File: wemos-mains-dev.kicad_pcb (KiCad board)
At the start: 2 copper layers, 74.2 x 46.5 mm, 15 parts, among them J1 Screw_Terminal_01x02, J2 Conn_02x12_Odd_Even, J8 SDA PU, J9 SDA PU, U1 AC-05-3, U2 WeMos_D1_mini

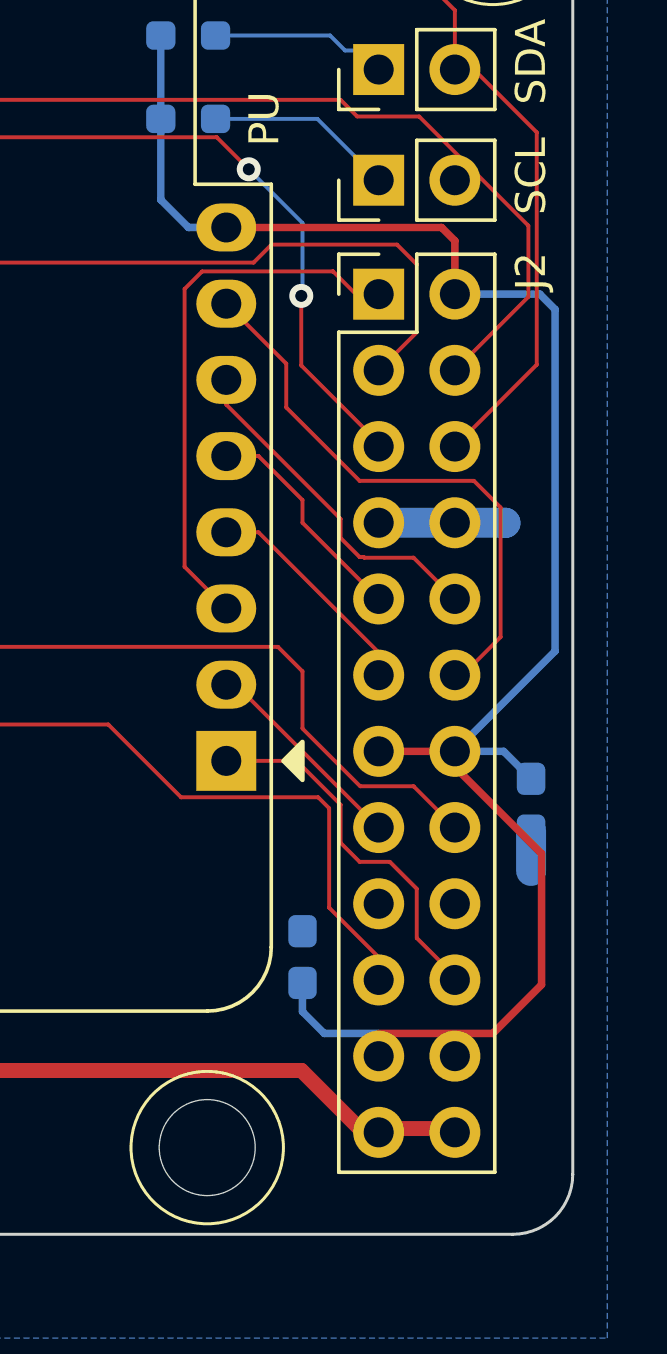
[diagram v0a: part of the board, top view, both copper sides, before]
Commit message: changed hat socket to socket from header
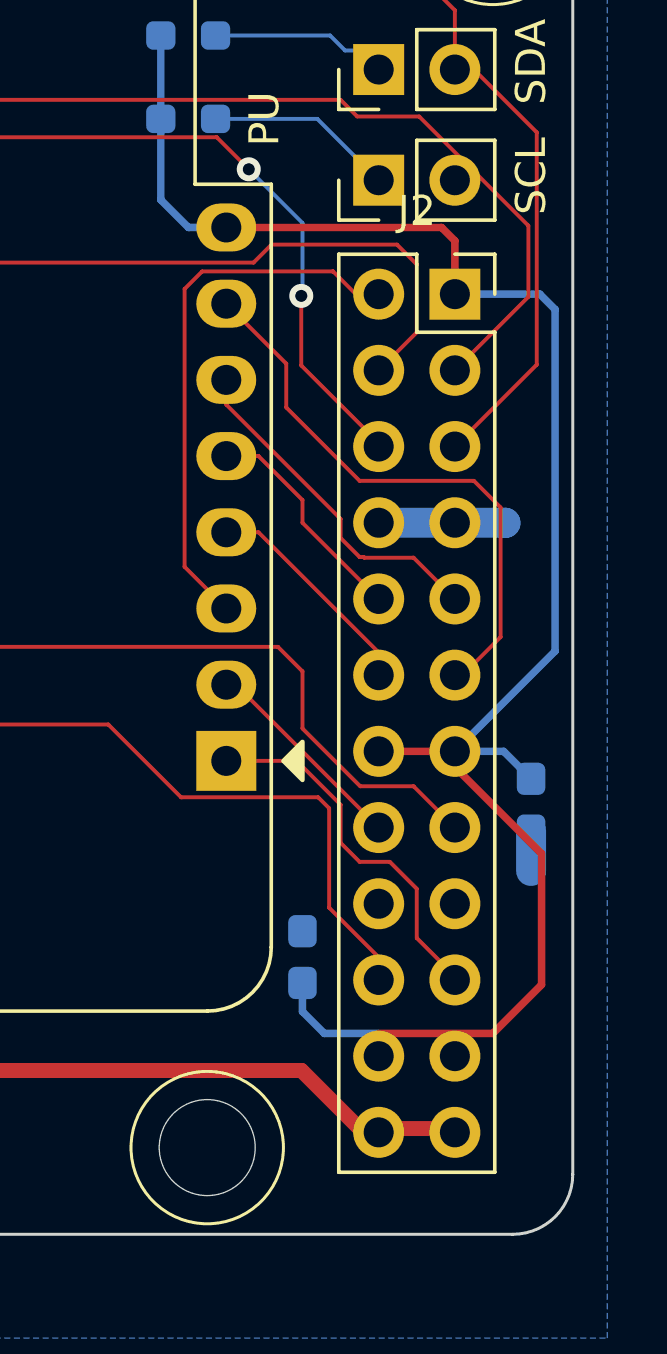
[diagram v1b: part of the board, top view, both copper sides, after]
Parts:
- J2: footprint Connector_PinHeader_2.54mm:PinHeader_2x12_P2.54mm_Vertical -> Connector_PinSocket_2.54mm:PinSocket_2x12_P2.54mm_Vertical
- moved J2 2.54 mm to (137.2, 87.1)
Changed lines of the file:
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@@
     (pad "" np_thru_hole circle (at 0 0) (size 3.2 3.2) (drill 3.2) (layers "*.Cu" "*.Mask"))
   )
-  (footprint "Connector_PinHeader_2.54mm:PinHeader_2x12_P2.54mm_Vertical" (layer "F.Cu")
-    (at 134.62 87.122)
-    (descr "Through hole straight pin header, 2x12, 2.54mm pitch, double rows")
-    (tags "Through hole pin header THT 2x12 2.54mm double row")
+  (footprint "Connector_PinSocket_2.54mm:PinSocket_2x12_P2.54mm_Vertical" (layer "F.Cu")
+    (at 137.16 87.122)
+    (descr "Through hole straight socket strip, 2x12, 2.54mm pitch, double cols (from Kicad 4.0.7), script generated")
+    (tags "Through hole socket strip THT 2x12 2.54mm double row")
     (property "Sheetfile" "wemos-mains-dev.kicad_sch")
     (property "Sheetname" "")
@@
     (property "ki_keywords" "connector")
     (attr through_hole)
-    (fp_text reference "J2" (at 5.08 -0.762 90) (layer "F.SilkS")
+    (fp_text reference "J2" (at -1.27 -2.77) (layer "F.SilkS")
         (effects (font (size 1 1) (thickness 0.15)))
     )
-    (fp_text value "Conn_02x12_Odd_Even" (at -3.65 30.318) (layer "F.Fab")
+    (fp_text value "Conn_02x12_Odd_Even" (at -1.27 30.71) (layer "F.Fab")
         (effects (font (size 1 1) (thickness 0.15)))
     )
-    (fp_text user "${REFERENCE}" (at 1.27 13.97 90) (layer "F.Fab")
+    (fp_text user "${REFERENCE}" (at -1.27 13.97 90) (layer "F.Fab")
         (effects (font (size 1 1) (thickness 0.15)))
     )
-    (fp_line (start -1.33 -1.33) (end 0 -1.33)
+    (fp_line (start -3.87 -1.33) (end -3.87 29.27)
       (stroke (width 0.12) (type solid)) (layer "F.SilkS"))
-    (fp_line (start -1.33 0) (end -1.33 -1.33)
+    (fp_line (start -3.87 -1.33) (end -1.27 -1.33)
       (stroke (width 0.12) (type solid)) (layer "F.SilkS"))
-    (fp_line (start -1.33 1.27) (end -1.33 29.27)
+    (fp_line (start -3.87 29.27) (end 1.33 29.27)
       (stroke (width 0.12) (type solid)) (layer "F.SilkS"))
-    (fp_line (start -1.33 1.27) (end 1.27 1.27)
+    (fp_line (start -1.27 -1.33) (end -1.27 1.27)
       (stroke (width 0.12) (type solid)) (layer "F.SilkS"))
-    (fp_line (start -1.33 29.27) (end 3.87 29.27)
+    (fp_line (start -1.27 1.27) (end 1.33 1.27)
       (stroke (width 0.12) (type solid)) (layer "F.SilkS"))
-    (fp_line (start 1.27 -1.33) (end 3.87 -1.33)
+    (fp_line (start 0 -1.33) (end 1.33 -1.33)
       (stroke (width 0.12) (type solid)) (layer "F.SilkS"))
-    (fp_line (start 1.27 1.27) (end 1.27 -1.33)
+    (fp_line (start 1.33 -1.33) (end 1.33 0)
       (stroke (width 0.12) (type solid)) (layer "F.SilkS"))
-    (fp_line (start 3.87 -1.33) (end 3.87 29.27)
+    (fp_line (start 1.33 1.27) (end 1.33 29.27)
       (stroke (width 0.12) (type solid)) (layer "F.SilkS"))
-    (fp_line (start -1.8 -1.8) (end -1.8 29.75)
+    (fp_line (start -4.34 -1.8) (end 1.76 -1.8)
       (stroke (width 0.05) (type solid)) (layer "F.CrtYd"))
-    (fp_line (start -1.8 29.75) (end 4.35 29.75)
+    (fp_line (start -4.34 29.7) (end -4.34 -1.8)
       (stroke (width 0.05) (type solid)) (layer "F.CrtYd"))
-    (fp_line (start 4.35 -1.8) (end -1.8 -1.8)
+    (fp_line (start 1.76 -1.8) (end 1.76 29.7)
       (stroke (width 0.05) (type solid)) (layer "F.CrtYd"))
-    (fp_line (start 4.35 29.75) (end 4.35 -1.8)
+    (fp_line (start 1.76 29.7) (end -4.34 29.7)
       (stroke (width 0.05) (type solid)) (layer "F.CrtYd"))
-    (fp_line (start -1.27 0) (end 0 -1.27)
+    (fp_line (start -3.81 -1.27) (end 0.27 -1.27)
       (stroke (width 0.1) (type solid)) (layer "F.Fab"))
-    (fp_line (start -1.27 29.21) (end -1.27 0)
+    (fp_line (start -3.81 29.21) (end -3.81 -1.27)
       (stroke (width 0.1) (type solid)) (layer "F.Fab"))
-    (fp_line (start 0 -1.27) (end 3.81 -1.27)
+    (fp_line (start 0.27 -1.27) (end 1.27 -0.27)
       (stroke (width 0.1) (type solid)) (layer "F.Fab"))
-    (fp_line (start 3.81 -1.27) (end 3.81 29.21)
+    (fp_line (start 1.27 -0.27) (end 1.27 29.21)
       (stroke (width 0.1) (type solid)) (layer "F.Fab"))
-    (fp_line (start 3.81 29.21) (end -1.27 29.21)
+    (fp_line (start 1.27 29.21) (end -3.81 29.21)
       (stroke (width 0.1) (type solid)) (layer "F.Fab"))
     (pad "1" thru_hole rect (at 0 0) (size 1.7 1.7) (drill 1) (layers "*.Cu" "*.Mask")
       (net 7 "D0_GPIO") (pinfunction "Pin_1") (pintype "passive"))
-    (pad "2" thru_hole oval (at 2.54 0) (size 1.7 1.7) (drill 1) (layers "*.Cu" "*.Mask")
+    (pad "2" thru_hole oval (at -2.54 0) (size 1.7 1.7) (drill 1) (layers "*.Cu" "*.Mask")
       (net 1 "+3.3V") (pinfunction "Pin_2") (pintype "passive"))
     (pad "3" thru_hole oval (at 0 2.54) (size 1.7 1.7) (drill 1) (layers "*.Cu" "*.Mask")
       (net 17 "RX") (pinfunction "Pin_3") (pintype "passive"))
-    (pad "4" thru_hole oval (at 2.54 2.54) (size 1.7 1.7) (drill 1) (layers "*.Cu" "*.Mask")
+    (pad "4" thru_hole oval (at -2.54 2.54) (size 1.7 1.7) (drill 1) (layers "*.Cu" "*.Mask")
       (net 15 "D1_SCL") (pinfunction "Pin_4") (pintype "passive"))
     (pad "5" thru_hole oval (at 0 5.08) (size 1.7 1.7) (drill 1) (layers "*.Cu" "*.Mask")
       (net 18 "TX") (pinfunction "Pin_5") (pintype "passive"))
-    (pad "6" thru_hole oval (at 2.54 5.08) (size 1.7 1.7) (drill 1) (layers "*.Cu" "*.Mask")
+    (pad "6" thru_hole oval (at -2.54 5.08) (size 1.7 1.7) (drill 1) (layers "*.Cu" "*.Mask")
       (net 16 "D2_SDA") (pinfunction "Pin_6") (pintype "passive"))
     (pad "7" thru_hole oval (at 0 7.62) (size 1.7 1.7) (drill 1) (layers "*.Cu" "*.Mask")
       (net 3 "GND") (pinfunction "Pin_7") (pintype "passive"))
-    (pad "8" thru_hole oval (at 2.54 7.62) (size 1.7 1.7) (drill 1) (layers "*.Cu" "*.Mask")
+    (pad "8" thru_hole oval (at -2.54 7.62) (size 1.7 1.7) (drill 1) (layers "*.Cu" "*.Mask")
       (net 3 "GND") (pinfunction "Pin_8") (pintype "passive"))
     (pad "9" thru_hole oval (at 0 10.16) (size 1.7 1.7) (drill 1) (layers "*.Cu" "*.Mask")
       (net 10 "D6_MISO") (pinfunction "Pin_9") (pintype "passive"))
-    (pad "10" thru_hole oval (at 2.54 10.16) (size 1.7 1.7) (drill 1) (layers "*.Cu" "*.Mask")
+    (pad "10" thru_hole oval (at -2.54 10.16) (size 1.7 1.7) (drill 1) (layers "*.Cu" "*.Mask")
       (net 13 "D7_MOSI") (pinfunction "Pin_10") (pintype "passive"))
     (pad "11" thru_hole oval (at 0 12.7) (size 1.7 1.7) (drill 1) (layers "*.Cu" "*.Mask")
       (net 9 "D5_SCK") (pinfunction "Pin_11") (pintype "passive"))
-    (pad "12" thru_hole oval (at 2.54 12.7) (size 1.7 1.7) (drill 1) (layers "*.Cu" "*.Mask")
+    (pad "12" thru_hole oval (at -2.54 12.7) (size 1.7 1.7) (drill 1) (layers "*.Cu" "*.Mask")
       (net 14 "D8_CS") (pinfunction "Pin_12") (pintype "passive"))
     (pad "13" thru_hole oval (at 0 15.24) (size 1.7 1.7) (drill 1) (layers "*.Cu" "*.Mask")
       (net 1 "+3.3V") (pinfunction "Pin_13") (pintype "passive"))
-    (pad "14" thru_hole oval (at 2.54 15.24) (size 1.7 1.7) (drill 1) (layers "*.Cu" "*.Mask")
+    (pad "14" thru_hole oval (at -2.54 15.24) (size 1.7 1.7) (drill 1) (layers "*.Cu" "*.Mask")
       (net 1 "+3.3V") (pinfunction "Pin_14") (pintype "passive"))
     (pad "15" thru_hole oval (at 0 17.78) (size 1.7 1.7) (drill 1) (layers "*.Cu" "*.Mask")
       (net 21 "A0_ANL") (pinfunction "Pin_15") (pintype "passive"))
-    (pad "16" thru_hole oval (at 2.54 17.78) (size 1.7 1.7) (drill 1) (layers "*.Cu" "*.Mask")
+    (pad "16" thru_hole oval (at -2.54 17.78) (size 1.7 1.7) (drill 1) (layers "*.Cu" "*.Mask")
       (net 12 "D4_LED") (pinfunction "Pin_16") (pintype "passive"))
     (pad "17" thru_hole oval (at 0 20.32) (size 1.7 1.7) (drill 1) (layers "*.Cu" "*.Mask")
       (net 3 "GND") (pinfunction "Pin_17") (pintype "passive"))
-    (pad "18" thru_hole oval (at 2.54 20.32) (size 1.7 1.7) (drill 1) (layers "*.Cu" "*.Mask")
+    (pad "18" thru_hole oval (at -2.54 20.32) (size 1.7 1.7) (drill 1) (layers "*.Cu" "*.Mask")
       (net 3 "GND") (pinfunction "Pin_18") (pintype "passive"))
     (pad "19" thru_hole oval (at 0 22.86) (size 1.7 1.7) (drill 1) (layers "*.Cu" "*.Mask")
       (net 8 "D3_ONE") (pinfunction "Pin_19") (pintype "passive"))
-    (pad "20" thru_hole oval (at 2.54 22.86) (size 1.7 1.7) (drill 1) (layers "*.Cu" "*.Mask")
+    (pad "20" thru_hole oval (at -2.54 22.86) (size 1.7 1.7) (drill 1) (layers "*.Cu" "*.Mask")
       (net 11 "RST") (pinfunction "Pin_20") (pintype "passive"))
     (pad "21" thru_hole oval (at 0 25.4) (size 1.7 1.7) (drill 1) (layers "*.Cu" "*.Mask")
       (net 1 "+3.3V") (pinfunction "Pin_21") (pintype "passive"))
-    (pad "22" thru_hole oval (at 2.54 25.4) (size 1.7 1.7) (drill 1) (layers "*.Cu" "*.Mask")
+    (pad "22" thru_hole oval (at -2.54 25.4) (size 1.7 1.7) (drill 1) (layers "*.Cu" "*.Mask")
       (net 1 "+3.3V") (pinfunction "Pin_22") (pintype "passive"))
     (pad "23" thru_hole oval (at 0 27.94) (size 1.7 1.7) (drill 1) (layers "*.Cu" "*.Mask")
       (net 4 "+5V") (pinfunction "Pin_23") (pintype "passive"))
-    (pad "24" thru_hole oval (at 2.54 27.94) (size 1.7 1.7) (drill 1) (layers "*.Cu" "*.Mask")
+    (pad "24" thru_hole oval (at -2.54 27.94) (size 1.7 1.7) (drill 1) (layers "*.Cu" "*.Mask")
       (net 4 "+5V") (pinfunction "Pin_24") (pintype "passive"))
-    (model "${KICAD6_3DMODEL_DIR}/Connector_PinHeader_2.54mm.3dshapes/PinHeader_2x12_P2.54mm_Vertical.wrl"
+    (model "${KICAD6_3DMODEL_DIR}/Connector_PinSocket_2.54mm.3dshapes/PinSocket_2x12_P2.54mm_Vertical.wrl"
       (offset (xyz 0 0 0))
       (scale (xyz 1 1 1))
